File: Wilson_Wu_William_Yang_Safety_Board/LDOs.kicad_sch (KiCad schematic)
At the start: 9 parts, among them U7 LM1117IDTX-3.3/NOPB, U8 LM1117IDTX-3.3/NOPB

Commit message: schematic done
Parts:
- added TP27: TestPoint, TestPoint:TestPoint_Pad_D1.0mm, symbol Connector:TestPoint
- TP17, TP18, TP19: footprint TestPoint:TestPoint_Loop_D2.54mm_Drill1.5mm_Beaded -> TestPoint:TestPoint_Pad_D1.0mm
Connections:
- net +12V: now also TP27.1
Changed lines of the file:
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@@
 		(color 0 0 0 0)
 	)
+	(junction
+		(at 36.83 34.29)
+		(diameter 0)
+		(color 0 0 0 0)
+	)
 	(wire
 		(pts
@@
 	(wire
 		(pts
+			(xy 36.83 34.29) (xy 36.83 44.45)
+		)
+		(stroke
+			(width 0)
+			(type default)
+		)
+	)
+	(wire
+		(pts
 			(xy 96.52 60.96) (xy 96.52 63.5)
 		)
@@
 	(wire
 		(pts
-			(xy 36.83 27.94) (xy 36.83 44.45)
+			(xy 36.83 27.94) (xy 36.83 34.29)
 		)
 		(stroke
@@
 			)
 		)
-		(property "Footprint" "TestPoint:TestPoint_Loop_D2.54mm_Drill1.5mm_Beaded"
+		(property "Footprint" "TestPoint:TestPoint_Pad_D1.0mm"
 			(at 96.52 66.04 0)
 			(effects
@@
 			)
 		)
-		(property "Footprint" "TestPoint:TestPoint_Loop_D2.54mm_Drill1.5mm_Beaded"
+		(property "Footprint" "TestPoint:TestPoint_Pad_D1.0mm"
 			(at 35.56 67.31 0)
 			(effects
@@
 			)
 		)
-		(property "Footprint" "TestPoint:TestPoint_Loop_D2.54mm_Drill1.5mm_Beaded"
+		(property "Footprint" "TestPoint:TestPoint_Pad_D1.0mm"
 			(at 97.79 35.56 0)
 			(effects
@@
 					(unit 1)
 				)
+			)
+		)
+	)
+	(symbol
+		(lib_id "Connector:TestPoint")
+		(at 36.83 34.29 90)
+		(unit 1)
+		(exclude_from_sim no)
+		(in_bom yes)
+		(on_board yes)
+		(dnp no)
+		(fields_autoplaced yes)
+		(property "Reference" "TP27"
+			(at 33.528 29.21 90)
+			(effects
+				(font
+					(size 1.27 1.27)
+				)
+			)
+		)
+		(property "Value" "TestPoint"
+			(at 33.528 31.75 90)
+			(effects
+				(font
+					(size 1.27 1.27)
+				)
+			)
+		)
+		(property "Footprint" "TestPoint:TestPoint_Pad_D1.0mm"
+			(at 36.83 29.21 0)
+			(effects
+				(font
+					(size 1.27 1.27)
+				)
+				(hide yes)
+			)
+		)
+		(property "Datasheet" "~"
+			(at 36.83 29.21 0)
+			(effects
+				(font
+					(size 1.27 1.27)
+				)
+				(hide yes)
+			)
+		)
+		(property "Description" "test point"
+			(at 36.83 34.29 0)
+			(effects
+				(font
+					(size 1.27 1.27)
+				)
+				(hide yes)
+			)
+		)
+		(pin "1"
+		)
+		(instances
+			(project "Wilson_Wu_William_Yang_Safety_Board"
+				(path "/fa857c32-0741-4b91-b122-1a57686bb514/b2ba9052-388b-4c74-b799-940f541ae929"
+					(reference "TP27")
+					(unit 1)
+				)

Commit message: hydrogen
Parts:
- removed TP19, TP27: TestPoint, TestPoint:TestPoint_Pad_D1.0mm, symbol Connector:TestPoint
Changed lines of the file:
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@@
 		(color 0 0 0 0)
 	)
-	(junction
-		(at 35.56 72.39)
-		(diameter 0)
-		(color 0 0 0 0)
-	)
-	(junction
-		(at 36.83 34.29)
-		(diameter 0)
-		(color 0 0 0 0)
-	)
 	(wire
 		(pts
@@
 	(wire
 		(pts
-			(xy 36.83 34.29) (xy 36.83 44.45)
+			(xy 36.83 27.94) (xy 36.83 44.45)
 		)
 		(stroke
@@
 	(wire
 		(pts
-			(xy 35.56 80.01) (xy 35.56 72.39)
-		)
-		(stroke
-			(width 0)
-			(type default)
-		)
-	)
-	(wire
-		(pts
 			(xy 36.83 27.94) (xy 45.72 27.94)
 		)
@@
 	(wire
 		(pts
-			(xy 36.83 27.94) (xy 36.83 34.29)
-		)
-		(stroke
-			(width 0)
-			(type default)
-		)
-	)
-	(wire
-		(pts
 			(xy 91.44 80.01) (xy 91.44 83.82)
 		)
@@
 	(wire
 		(pts
-			(xy 35.56 72.39) (xy 35.56 63.5)
+			(xy 35.56 63.5) (xy 35.56 80.01)
 		)
 		(stroke
@@
 	)
 	(symbol
-		(lib_id "Connector:TestPoint")
-		(at 35.56 72.39 90)
-		(unit 1)
-		(exclude_from_sim no)
-		(in_bom yes)
-		(on_board yes)
-		(dnp no)
-		(fields_autoplaced yes)
-		(property "Reference" "TP19"
-			(at 32.258 67.31 90)
-			(effects
-				(font
-					(size 1.27 1.27)
-				)
-			)
-		)
-		(property "Value" "TestPoint"
-			(at 32.258 69.85 90)
-			(effects
-				(font
-					(size 1.27 1.27)
-				)
-			)
-		)
-		(property "Footprint" "TestPoint:TestPoint_Pad_D1.0mm"
-			(at 35.56 67.31 0)
-			(effects
-				(font
-					(size 1.27 1.27)
-				)
-				(hide yes)
-			)
-		)
-		(property "Datasheet" "~"
-			(at 35.56 67.31 0)
-			(effects
-				(font
-					(size 1.27 1.27)
-				)
-				(hide yes)
-			)
-		)
-		(property "Description" "test point"
-			(at 35.56 72.39 0)
-			(effects
-				(font
-					(size 1.27 1.27)
-				)
-				(hide yes)
-			)
-		)
-		(pin "1"
-		)
-		(instances
-			(project "Wilson_Wu_William_Yang_Safety_Board"
-				(path "/fa857c32-0741-4b91-b122-1a57686bb514/b2ba9052-388b-4c74-b799-940f541ae929"
-					(reference "TP19")
-					(unit 1)
-				)
-			)
-		)
-	)
-	(symbol
 		(lib_id "lm1117:LM1117IDTX-3.3_NOPB")
 		(at 67.31 66.04 0)
@@
 					(unit 1)
 				)
-			)
-		)
-	)
-	(symbol
-		(lib_id "Connector:TestPoint")
-		(at 36.83 34.29 90)
-		(unit 1)
-		(exclude_from_sim no)
-		(in_bom yes)
-		(on_board yes)
-		(dnp no)
-		(fields_autoplaced yes)
-		(property "Reference" "TP27"
-			(at 33.528 29.21 90)
-			(effects
-				(font
-					(size 1.27 1.27)
-				)
-			)
-		)
-		(property "Value" "TestPoint"
-			(at 33.528 31.75 90)
-			(effects
-				(font
-					(size 1.27 1.27)
-				)
-			)
-		)
-		(property "Footprint" "TestPoint:TestPoint_Pad_D1.0mm"
-			(at 36.83 29.21 0)
-			(effects
-				(font
-					(size 1.27 1.27)
-				)
-				(hide yes)
-			)
-		)
-		(property "Datasheet" "~"
-			(at 36.83 29.21 0)
-			(effects
-				(font
-					(size 1.27 1.27)
-				)
-				(hide yes)
-			)
-		)
-		(property "Description" "test point"
-			(at 36.83 34.29 0)
-			(effects
-				(font
-					(size 1.27 1.27)
-				)
-				(hide yes)
-			)
-		)
-		(pin "1"
-		)
-		(instances
-			(project "Wilson_Wu_William_Yang_Safety_Board"
-				(path "/fa857c32-0741-4b91-b122-1a57686bb514/b2ba9052-388b-4c74-b799-940f541ae929"
-					(reference "TP27")
-					(unit 1)
-				)

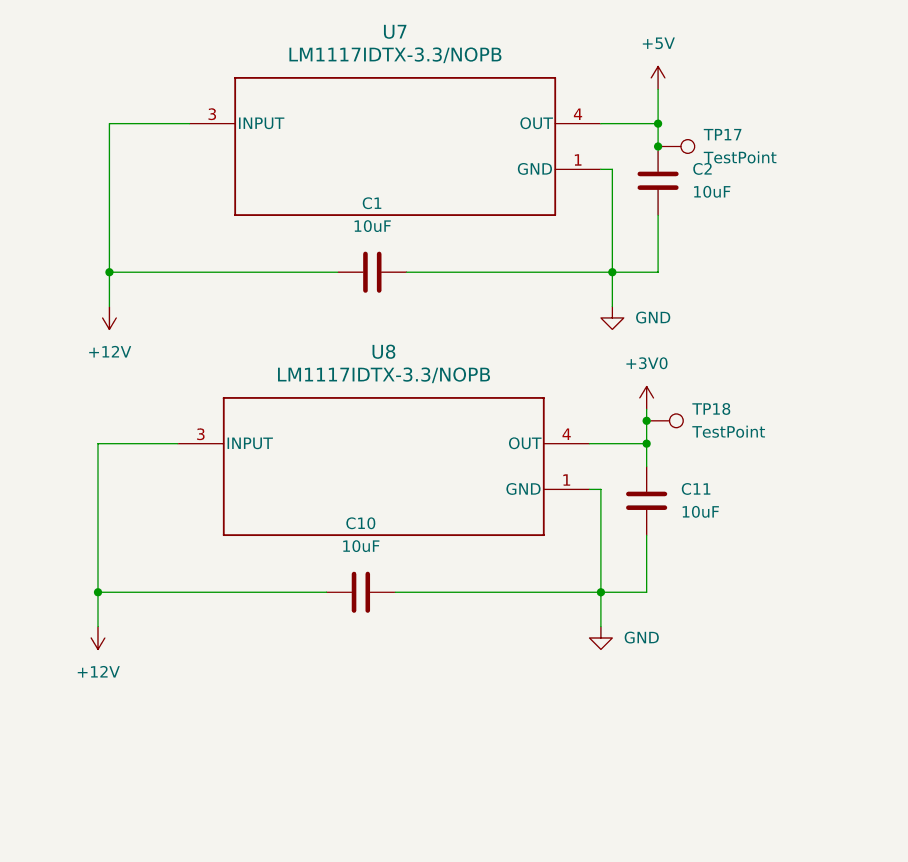
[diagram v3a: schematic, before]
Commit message: changed ldo
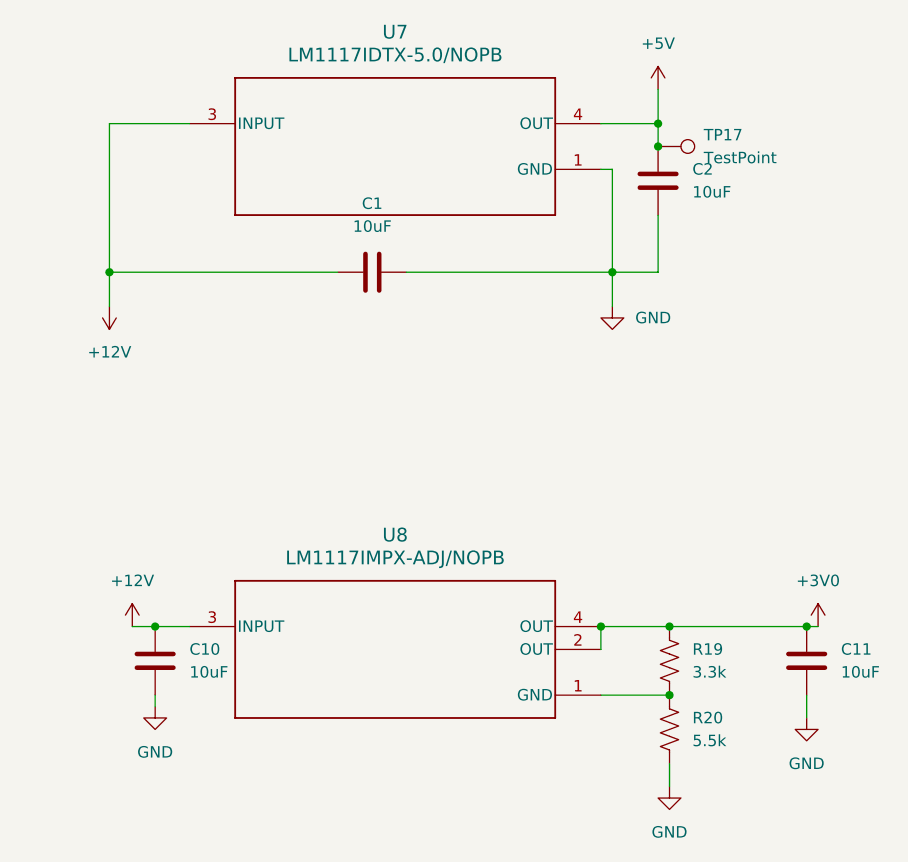
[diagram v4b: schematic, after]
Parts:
- removed TP18: TestPoint, TestPoint:TestPoint_Pad_D1.0mm, symbol Connector:TestPoint
- removed U8: LM1117IDTX-3.3/NOPB, ul_LM1117IDTX-3-3-NOPB:NDP0003B, symbol lm1117:LM1117IDTX-3.3_NOPB
- added R19: 3.3k, Resistor_SMD:R_0805_2012Metric, symbol Device:R_US
- added R20: 5.5k, Resistor_SMD:R_0805_2012Metric, symbol Device:R_US
- added U8: LM1117IMPX-ADJ/NOPB, adj ldo:DCY0004A_M, symbol adj ldo:LM1117IMPX-ADJ_NOPB
- U7: value LM1117IDTX-3.3/NOPB -> LM1117IDTX-5.0/NOPB
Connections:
- net +12V: now also C10.2, U8.3 (INPUT); no longer C10.1
- net +3V0: now also R19.1, U8.2 (OUT), U8.4 (OUT)
- net GND: now also C10.1, R20.2; no longer C10.2
- new net: R19.2, R20.1, U8.1 (GND)

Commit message: bruh
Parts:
- R20: value 5.5k -> 4.7k
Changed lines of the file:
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@@
 			)
 		)
-		(property "Value" "5.5k"
+		(property "Value" "4.7k"
 			(at 101.6 96.5199 0)
 			(effects

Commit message: layout
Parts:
- added ADJ_LDO_TP1: V_DIVIDED, TestPoint:TestPoint_Pad_D1.0mm, symbol Connector:TestPoint
- TP17: value TestPoint -> 5V0_LDO_TP
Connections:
- net +3V0: now also ADJ_LDO_TP1.1
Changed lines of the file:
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@@
+	)
+	(junction
+		(at 105.41 83.82)
+		(diameter 0)
+		(color 0 0 0 0)
 	)
 	(junction
@@
 	(wire
 		(pts
+			(xy 105.41 83.82) (xy 114.3 83.82)
+		)
+		(stroke
+			(width 0)
+			(type default)
+		)
+	)
+	(wire
+		(pts
 			(xy 92.71 33.02) (xy 91.44 33.02)
 		)
@@
 	(wire
 		(pts
-			(xy 99.06 83.82) (xy 114.3 83.82)
+			(xy 99.06 83.82) (xy 105.41 83.82)
 		)
 		(stroke
@@
 		(pts
 			(xy 99.06 101.6) (xy 99.06 99.06)
+		)
+		(stroke
+			(width 0)
+			(type default)
+		)
+	)
+	(wire
+		(pts
+			(xy 105.41 82.55) (xy 105.41 83.82)
 		)
 		(stroke
@@
 			)
 		)
-		(property "Value" "TestPoint"
+		(property "Value" "5V0_LDO_TP"
 			(at 102.87 31.7499 90)
 			(effects
@@
 					(unit 1)
 				)
+			)
+		)
+	)
+	(symbol
+		(lib_id "Connector:TestPoint")
+		(at 105.41 82.55 0)
+		(unit 1)
+		(exclude_from_sim no)
+		(in_bom yes)
+		(on_board yes)
+		(dnp no)
+		(property "Reference" "ADJ_LDO_TP1"
+			(at 99.06 76.454 0)
+			(effects
+				(font
+					(size 1.27 1.27)
+				)
+				(justify left)
+			)
+		)
+		(property "Value" "V_DIVIDED"
+			(at 107.95 80.5179 0)
+			(effects
+				(font
+					(size 1.27 1.27)
+				)
+				(justify left)
+				(hide yes)
+			)
+		)
+		(property "Footprint" "TestPoint:TestPoint_Pad_D1.0mm"
+			(at 110.49 82.55 0)
+			(effects
+				(font
+					(size 1.27 1.27)
+				)
+				(hide yes)
+			)
+		)
+		(property "Datasheet" "~"
+			(at 110.49 82.55 0)
+			(effects
+				(font
+					(size 1.27 1.27)
+				)
+				(hide yes)
+			)
+		)
+		(property "Description" "test point"
+			(at 105.41 82.55 0)
+			(effects
+				(font
+					(size 1.27 1.27)
+				)
+				(hide yes)
+			)
+		)
+		(pin "1"
+		)
+		(instances
+			(project "Wilson_Wu_William_Yang_Safety_Board"
+				(path "/fa857c32-0741-4b91-b122-1a57686bb514/b2ba9052-388b-4c74-b799-940f541ae929"
+					(reference "ADJ_LDO_TP1")
+					(unit 1)
+				)
